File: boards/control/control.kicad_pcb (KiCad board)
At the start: 2 copper layers, 100 x 100 mm, 75 parts, among them J1 61304021021, U1 SN74ACT08PW, U10 MC74ACT139DG, U11 SN74ACT08PW, U12 SN74ACT08PW, U13 SN74ACT32PW, U14 74ACT00MTCX, U15 MC74ACT139DG, U16 SN74ACT32PW, U2 MC74ACT139DG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

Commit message: Add license information
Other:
- board text added: "Licensed under the TAPR OHL (www.tapr.org/OHL)"
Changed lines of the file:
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@@
   (general
     (thickness 1.6)
-    (drawings 40)
+    (drawings 41)
     (tracks 1537)
     (zones 0)
@@
     (date 2020-03-22)
     (rev 2)
+    (comment 1 "Licensed under the TAPR Open Hardware License (www.tapr.org/OHL)")
   )
   (layers
@@
   )
   (setup
-    (last_trace_width 0.4)
+    (last_trace_width 0.2)
     (user_trace_width 0.2)
     (user_trace_width 0.4)
@@
     )
   )
+  (gr_text "Licensed under the TAPR OHL\n(www.tapr.org/OHL)" (at 149.6 87.6) (layer B.SilkS)
+    (effects (font (size 1 1) (thickness 0.15)) (justify mirror))
+  )
   (gr_text we_cycle (at 161 129.8 90) (layer F.SilkS)

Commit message: Control: PCB rev. 3
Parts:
- added C11: 0.1u, Capacitor_SMD:C_0805_2012Metric, F.Cu at (135.6, 93.4)
- added C12: 0.1u, Capacitor_SMD:C_0805_2012Metric, F.Cu at (151.2, 93.4)
- added C13: 0.1u, Capacitor_SMD:C_0805_2012Metric, F.Cu at (166.8, 93.4)
- added C14: 0.1u, Capacitor_SMD:C_0805_2012Metric, F.Cu at (182.4, 93.4)
- added C15: 0.1u, Capacitor_SMD:C_0805_2012Metric, F.Cu at (120.1, 111.5)
- added C16: 0.1u, Capacitor_SMD:C_0805_2012Metric, F.Cu at (135.7, 111.6)
- added C17: 0.1u, Capacitor_SMD:C_0805_2012Metric, F.Cu at (151.3, 111.6)
- added C18: 0.1u, Capacitor_SMD:C_0805_2012Metric, F.Cu at (166.9, 111.6)
- added C19: 0.1u, Capacitor_SMD:C_0805_2012Metric, F.Cu at (182.7, 111.6)
- added D23: KP-2012EC, LED_SMD:LED_0805_2012Metric, F.Cu at (109.1, 132.0)
- added D24: KP-2012CGCK, LED_SMD:LED_0805_2012Metric, F.Cu at (162.9, 132.1)
- added R23: 620, Resistor_SMD:R_0805_2012Metric, F.Cu at (109.1, 136.0)
- added R24: 50, Resistor_SMD:R_0805_2012Metric, F.Cu at (124.7, 101.3)
- added R25: 1k, Resistor_SMD:R_0805_2012Metric, F.Cu at (105.1, 92.4)
- added R26: 50, Resistor_SMD:R_0805_2012Metric, F.Cu at (124.9, 53.5)
- added R27: 600, Resistor_SMD:R_0805_2012Metric, F.Cu at (162.9, 136.0)
- added U17: SN74LV74APW, Package_SO:TSSOP-14_4.4x5mm_P0.65mm, F.Cu at (170.8, 77.2)
- added U18: SN74LV02APWR, Package_SO:TSSOP-14_4.4x5mm_P0.65mm, F.Cu at (186.4, 77.2)
- C4: value 10u 6.3v -> TPSB336K010T0425; footprint Capacitor_SMD:CP_Elec_4x4.5 -> Capacitor_Tantalum_SMD:CP_EIA-3528-21_Kemet-B_Pad1.50x2.35mm_HandSolder
- U1, U11, U12: value SN74ACT08PW -> 74LV08APWJ
- U10, U15, U2: value MC74ACT139DG -> SN74LV139APWR; footprint Package_SO:SOIC-16_3.9x9.9mm_P1.27mm -> Package_SO:TSSOP-16_4.4x5mm_P0.65mm
- U13, U16, U5, U8: value SN74ACT32PW -> 74LV32APWJ
- U14, U9: value 74ACT00MTCX -> SN74LV00APW
- U3: value MC74ACT86DG -> SN74LV86APWR; footprint Package_SO:SOIC-14_3.9x8.7mm_P1.27mm -> Package_SO:TSSOP-14_4.4x5mm_P0.65mm
- U4, U6: value SN74ACT74D -> SN74LV74APW; footprint Package_SO:SOIC-14_3.9x8.7mm_P1.27mm -> Package_SO:TSSOP-14_4.4x5mm_P0.65mm
- U7: value SN74ACT04PW -> SN74LV04APWR
- moved C10 75.5 mm to (120.1, 93.4)
- moved C3 67.3 mm to (174.0, 57.6)
- moved U1 62.9 mm to (177.9, 59.8)
- moved U4 61.5 mm to (124.0, 95.5)
- moved U11 53.8 mm to (186.4, 95.6)
- moved U3 47.3 mm to (139.6, 77.2)
- moved U10 46.3 mm to (155.3, 113.6)
- moved C5 44.5 mm to (120.0, 75.2)
- moved U8 44.5 mm to (124.0, 77.3)
- moved U6 43.4 mm to (139.6, 59.9)
- moved C9 39.2 mm to (182.4, 75.2)
- moved C6 29.3 mm to (135.7, 75.1)
- moved C7 26.0 mm to (151.2, 75.1)
- moved U15 22.5 mm to (139.6, 113.6)
- moved C8 21.8 mm to (166.9, 75.2)
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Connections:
- D20 pad 1: /~clk -> Net-(D20-Pad1)
- D21 pad 1: /~supercycle -> Net-(D21-Pad1)
- D21 pad 2: Net-(D21-Pad2) -> /supercycle
- D5 pad 2: /cycle -> /inc_ip
- J1 pad 26: Net-(J1-Pad26) -> /~mem_rdy
- J1 pad 7: /cycle -> /inc_ip
- R21 pad 1: VCC -> GND
- R21 pad 2: Net-(D21-Pad2) -> Net-(D21-Pad1)
- U14 pad 10: GND -> /~clk
- U14 pad 12: GND -> VCC
- U14 pad 13: GND -> VCC
- U14 pad 9: GND -> /~rst
- U16 pad 10: GND -> /~cycle
- U16 pad 12: GND -> VCC
- U16 pad 13: GND -> VCC
- U16 pad 9: GND -> /~op_st
- U3 pad 11: Net-(U3-Pad11) -> /we_cycle_d
- U3 pad 12: GND -> /~we_cycle
- U3 pad 13: GND -> /~cycle_flip_ena
- U3 pad 4: GND -> /~cycle
- U3 pad 5: GND -> /~cycle_flip_ena
- U3 pad 6: Net-(U3-Pad6) -> /cycle_d
- U4 pad 2: /~cycle -> /cycle_d
- U4 pad 5: /cycle -> Net-(R24-Pad2)
- U6 pad 12: /~we_cycle -> /we_cycle_d
- U7 pad 12: /~clk -> Net-(D20-Pad1)
- U9 pad 1: /~op_st -> Net-(U16-Pad8)
- U9 pad 2: /~cycle -> Net-(U16-Pad8)
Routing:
- net VCC: track 85.2 -> 830.4 mm, vias 2 -> 25
- net GND: track 96.3 -> 826.7 mm, vias 39 -> 46
- net /inc_ip: track 0.00 -> 142.1 mm, vias 0 -> 5
- net /mem_rdy: track 0.00 -> 131.1 mm, vias 0 -> 5
- net Net-(D20-Pad1): track 0.00 -> 107.6 mm, vias 0 -> 4
- net /cycle: track 198.1 -> 91.4 mm, vias 10 -> 9
- net /~mem_rdy: track 0.00 -> 95.8 mm, vias 0 -> 3
- net /clk: track 154.3 -> 66.0 mm, vias 7 -> 6
- net /ir2: track 156.4 -> 73.1 mm, vias 5 -> 6
- net /supercycle: track 0.00 -> 81.2 mm, vias 0 -> 2
- net /op_jmp: track 22.4 -> 102.7 mm, vias 2 -> 4
- net /~oe_alu_di: track 211.0 -> 141.8 mm, vias 8 -> 12
- net /~supercycle: track 140.1 -> 73.0 mm, vias 8 -> 4
- net /p_selector: track 121.5 -> 57.1 mm
- net /~cycle_flip_ena: track 0.00 -> 60.6 mm, vias 0 -> 3
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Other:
- rule trace_min: 0.2 -> 0.153
- board text added: "CU rev.3"
- board text added: "cycle_flip_ena"
- board text added: "mem_rdy"

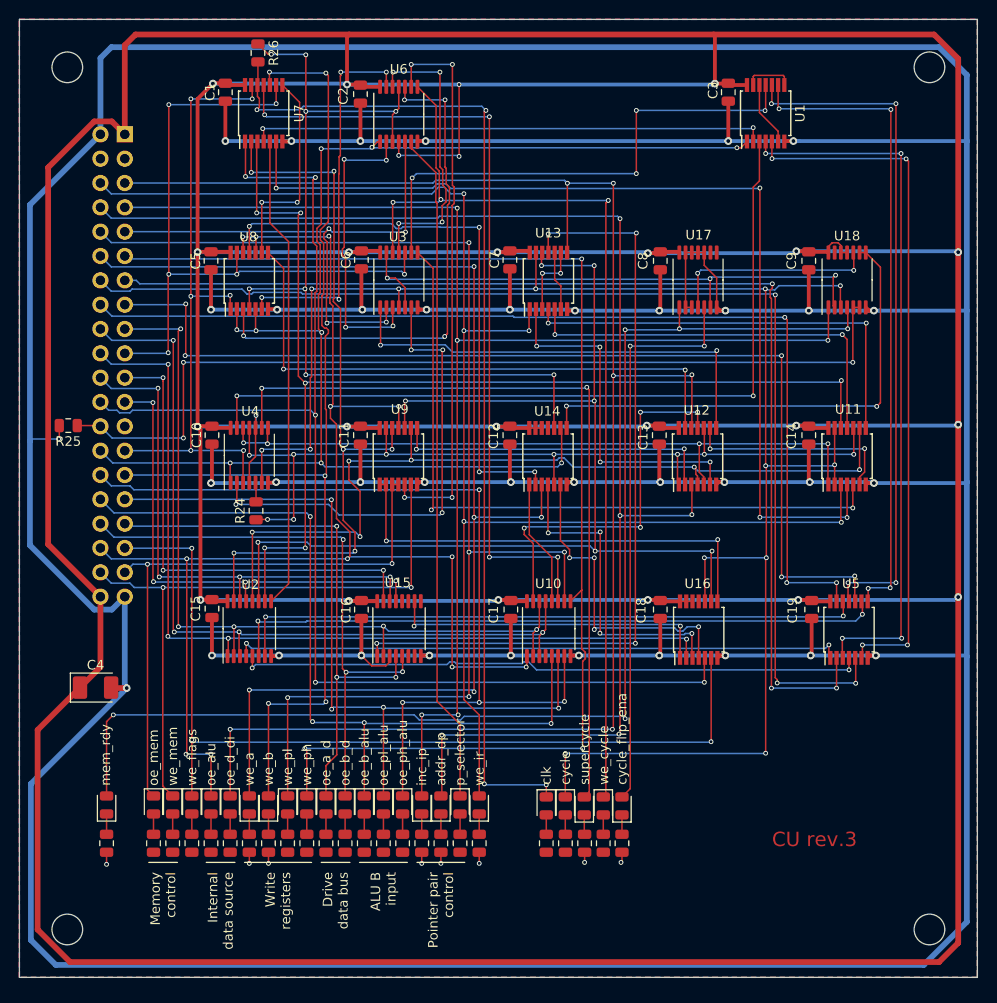
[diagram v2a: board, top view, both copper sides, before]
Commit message: Control: fix PCB
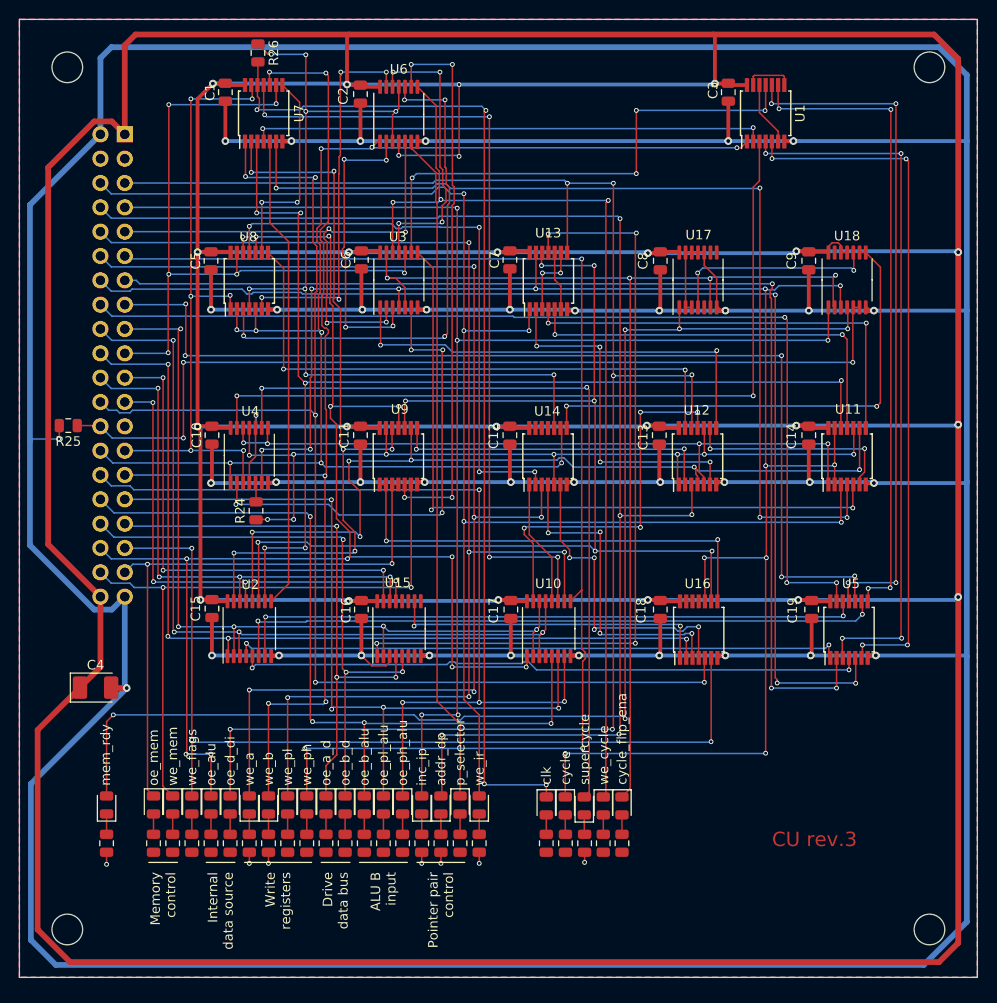
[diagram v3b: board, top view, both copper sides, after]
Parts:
- turned D24 to 270 degrees
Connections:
- net Net-(U10-Pad15) renamed /~we_x
- net Net-(U13-Pad11) renamed /~oe_reg_d
- net Net-(U14-Pad4) renamed /~is_mov
- net Net-(U17-Pad4) renamed /ff_rdy_n_sd
- D24 pad 1: Net-(D24-Pad1) -> /~cycle_flip_ena
- D24 pad 2: /cycle_flip_ena -> Net-(D24-Pad2)
- J1 pad 25: Net-(J1-Pad25) -> (no net)
- J1 pad 3: Net-(J1-Pad3) -> (no net)
- J1 pad 4: Net-(J1-Pad4) -> (no net)
- R27 pad 1: GND -> VCC
- R27 pad 2: Net-(D24-Pad1) -> Net-(D24-Pad2)
- U10 pad 4: Net-(U10-Pad4) -> (no net)
- U14 pad 11: Net-(U14-Pad11) -> (no net)
- U15 pad 11: Net-(U15-Pad11) -> (no net)
- U15 pad 12: Net-(U15-Pad12) -> (no net)
- U15 pad 6: Net-(U15-Pad6) -> (no net)
- U15 pad 7: Net-(U15-Pad7) -> (no net)
- U15 pad 9: Net-(U15-Pad9) -> (no net)
- U16 pad 11: Net-(U16-Pad11) -> (no net)
- U17 pad 5: /cycle_flip_ena -> (no net)
- U17 pad 8: Net-(U17-Pad8) -> (no net)
- U17 pad 9: Net-(U17-Pad9) -> (no net)
- U18 pad 13: Net-(U18-Pad13) -> (no net)
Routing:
- net /cycle_flip_ena: track 59.2 -> 0.00 mm, vias 2 -> 0
- net /~cycle_flip_ena: track 60.6 -> 115.1 mm, vias 3 -> 4
- net Net-(D24-Pad2): track 0.00 -> 2.03 mm
- net Net-(D24-Pad1): track 2.03 -> 0.00 mm
- net GND: track 826.7 -> 825.6 mm, vias 46 -> 45
